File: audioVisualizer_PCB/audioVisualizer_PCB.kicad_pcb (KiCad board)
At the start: 2 copper layers, 69 x 30.5 mm, 41 parts, among them J1 Microphone_Module, J10 Conn_01x08_Socket, J11 Conn_01x08_Socket, J12 Conn_01x08_Socket, J2 USB_B_Micro, J3 SPI_MATRIX, J4 JTAG, J5 Conn_01x08_Socket, J6 Conn_01x08_Socket, J7 Conn_01x08_Socket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

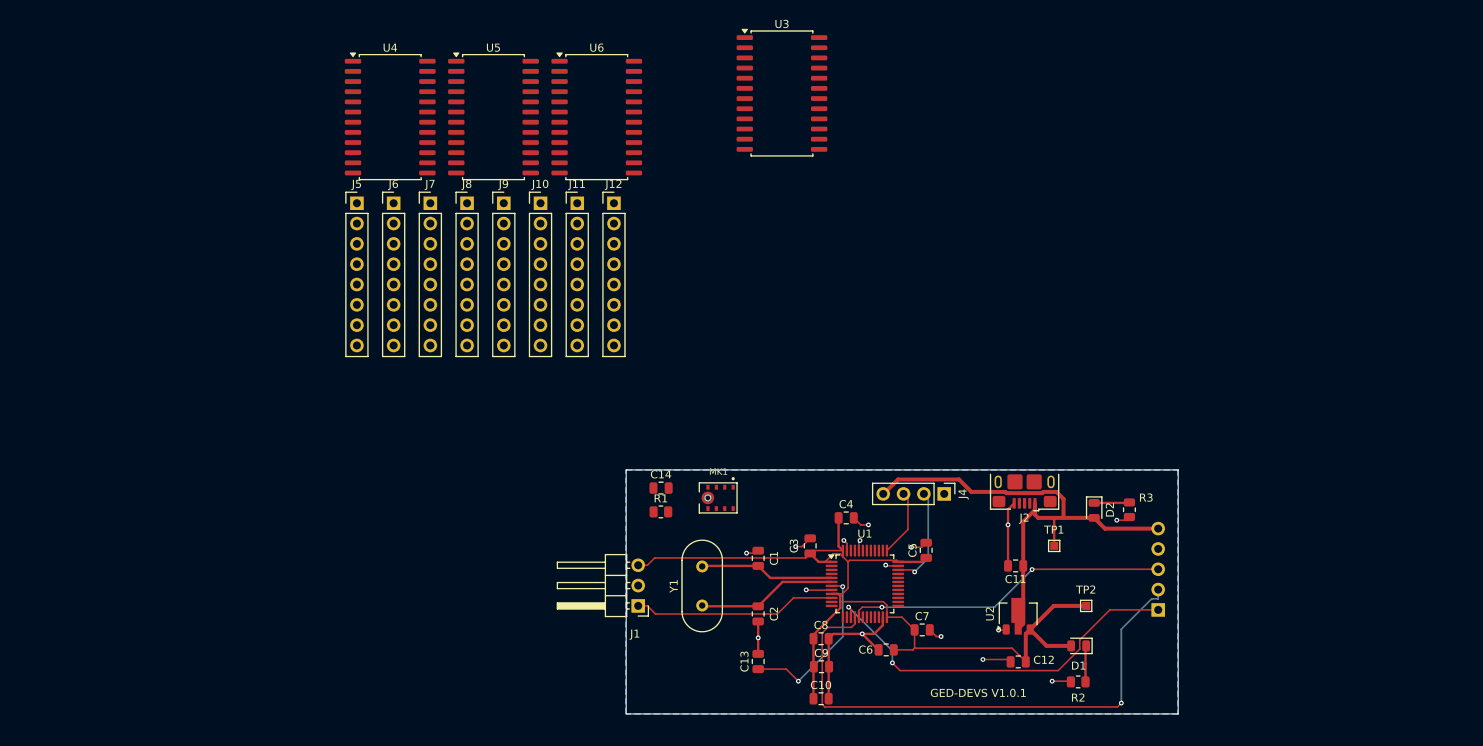
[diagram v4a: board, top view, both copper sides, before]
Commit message: migration to stm32f401
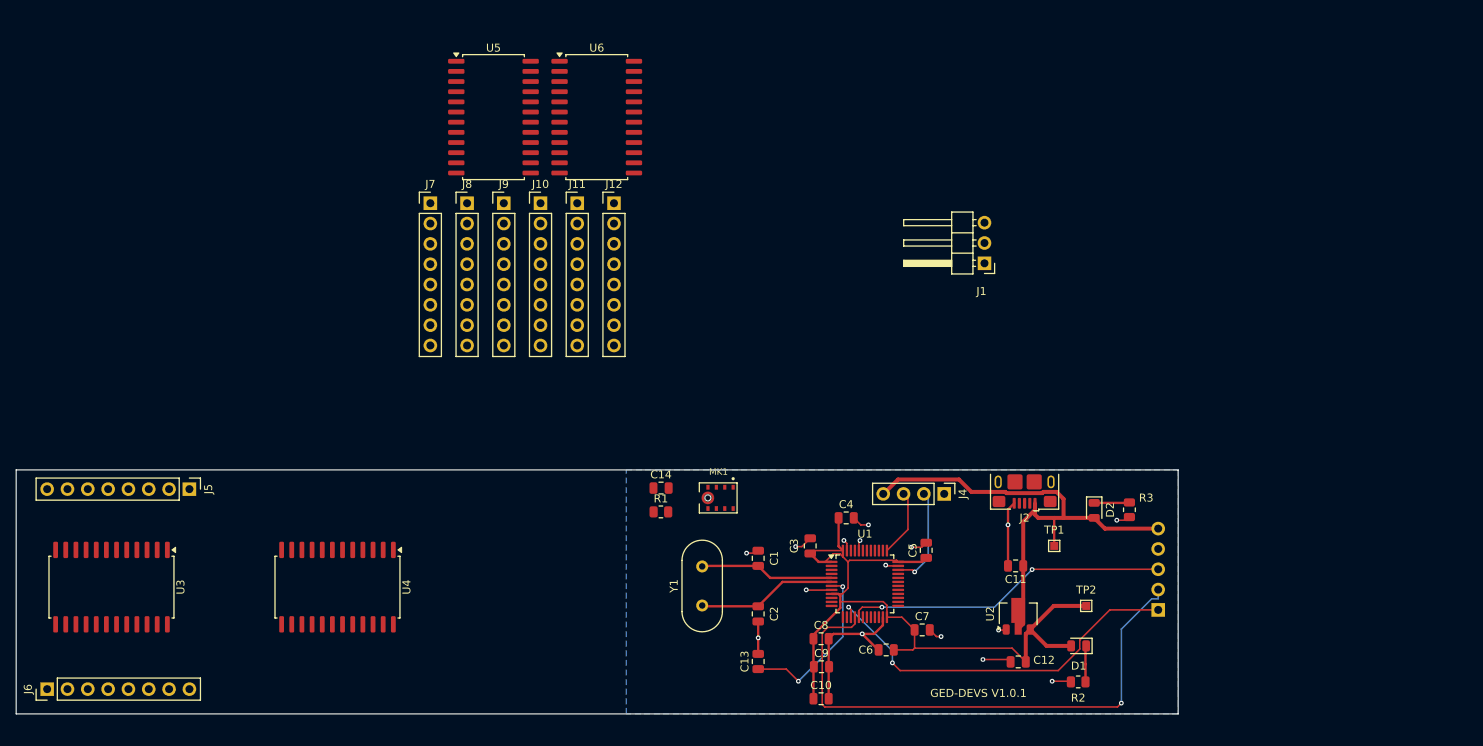
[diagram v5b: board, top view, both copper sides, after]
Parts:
- moved U3 104.1 mm to (26.2, 83.2), turned to -90 degrees
- moved J6 74.6 mm to (18.2, 96.0), turned to 90 degrees
- moved J1 60.9 mm to (135.4, 42.8)
- moved U4 59.1 mm to (54.5, 83.2), turned to -90 degrees
- moved J5 41.4 mm to (36.0, 71.0), turned to -90 degrees
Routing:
- net /OUT: track 25.4 -> 0.00 mm
- net +3.3V: track 117.8 -> 95.7 mm
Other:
- board size 69 x 30.5 mm -> 145.2 x 30.5 mm

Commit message: embeddeding the mcu is harder than I thought
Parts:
- added U7: STM32F401CCUx, Package_DFN_QFN:QFN-48-1EP_7x7mm_P0.5mm_EP5.6x5.6mm, F.Cu at (173.5, 57.2)
- added Y2: Crystal_GND23, Crystal:Crystal_SMD_3225-4Pin_3.2x2.5mm, F.Cu at (170.6, 67.7)
- moved U6 73.2 mm to (129.2, 84.3), turned to -90 degrees
- moved J12 69.5 mm to (119.7, 97.7), turned to 90 degrees
- moved C12 65.8 mm to (175.7, 37.6)
- moved C13 65.8 mm to (143.2, 37.6)
- moved C2 65.8 mm to (143.2, 31.6)
- moved C3 65.8 mm to (149.7, 23.1)
- moved C4 65.8 mm to (154.2, 19.6)
- moved C5 65.8 mm to (164.2, 23.7)
- moved C6 65.8 mm to (159.2, 36.1)
- moved C7 65.8 mm to (163.7, 33.6)
- moved C9 65.8 mm to (151.1, 38.2)
- moved D2 65.8 mm to (185.2, 18.7)
- moved J2 65.8 mm to (176.5, 15.1)
- moved J3 65.8 mm to (193.2, 31.1)
- moved J4 65.8 mm to (166.5, 16.6)
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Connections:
- C1 pad 2: Net-(U1-PD0) -> unconnected-(C1-Pad2)
- C13 pad 1: Net-(U1-NRST) -> unconnected-(C13-Pad1)
- C2 pad 1: Net-(U1-PD1) -> unconnected-(C2-Pad1)
- J10 pad 1: Net-(J10-Pin_1) -> Net-(J6-Pin_1)
- J10 pad 2: Net-(J10-Pin_2) -> Net-(J6-Pin_2)
- J10 pad 3: Net-(J10-Pin_3) -> Net-(J6-Pin_3)
- J10 pad 4: Net-(J10-Pin_4) -> Net-(J6-Pin_4)
- J10 pad 5: Net-(J10-Pin_5) -> Net-(J6-Pin_5)
- J10 pad 6: Net-(J10-Pin_6) -> Net-(J6-Pin_6)
- J10 pad 7: Net-(J10-Pin_7) -> Net-(J6-Pin_7)
- J10 pad 8: Net-(J10-Pin_8) -> Net-(J6-Pin_8)
- J11 pad 1: Net-(J11-Pin_1) -> Net-(J5-Pin_1)
- J11 pad 2: Net-(J11-Pin_2) -> Net-(J5-Pin_2)
- J11 pad 3: Net-(J11-Pin_3) -> Net-(J5-Pin_3)
- J11 pad 4: Net-(J11-Pin_4) -> Net-(J5-Pin_4)
- J11 pad 5: Net-(J11-Pin_5) -> Net-(J5-Pin_5)
- J11 pad 6: Net-(J11-Pin_6) -> Net-(J5-Pin_6)
- J11 pad 7: Net-(J11-Pin_7) -> Net-(J5-Pin_7)
- J11 pad 8: Net-(J11-Pin_8) -> Net-(J5-Pin_8)
- J12 pad 1: Net-(J12-Pin_1) -> Net-(J6-Pin_1)
- J12 pad 2: Net-(J12-Pin_2) -> Net-(J6-Pin_2)
- J12 pad 3: Net-(J12-Pin_3) -> Net-(J6-Pin_3)
- J12 pad 4: Net-(J12-Pin_4) -> Net-(J6-Pin_4)
- J12 pad 5: Net-(J12-Pin_5) -> Net-(J6-Pin_5)
- J12 pad 6: Net-(J12-Pin_6) -> Net-(J6-Pin_6)
- J12 pad 7: Net-(J12-Pin_7) -> Net-(J6-Pin_7)
- J12 pad 8: Net-(J12-Pin_8) -> Net-(J6-Pin_8)
- J7 pad 1: Net-(J7-Pin_1) -> Net-(J5-Pin_1)
- J7 pad 2: Net-(J7-Pin_2) -> Net-(J5-Pin_2)
- J7 pad 3: Net-(J7-Pin_3) -> Net-(J5-Pin_3)
- J7 pad 4: Net-(J7-Pin_4) -> Net-(J5-Pin_4)
- J7 pad 5: Net-(J7-Pin_5) -> Net-(J5-Pin_5)
- J7 pad 6: Net-(J7-Pin_6) -> Net-(J5-Pin_6)
- J7 pad 7: Net-(J7-Pin_7) -> Net-(J5-Pin_7)
- J7 pad 8: Net-(J7-Pin_8) -> Net-(J5-Pin_8)
- J8 pad 1: Net-(J8-Pin_1) -> Net-(J6-Pin_1)
- J8 pad 2: Net-(J8-Pin_2) -> Net-(J6-Pin_2)
- J8 pad 3: Net-(J8-Pin_3) -> Net-(J6-Pin_3)
- J8 pad 4: Net-(J8-Pin_4) -> Net-(J6-Pin_4)
- J8 pad 5: Net-(J8-Pin_5) -> Net-(J6-Pin_5)
- J8 pad 6: Net-(J8-Pin_6) -> Net-(J6-Pin_6)
- J8 pad 7: Net-(J8-Pin_7) -> Net-(J6-Pin_7)
- J8 pad 8: Net-(J8-Pin_8) -> Net-(J6-Pin_8)
- J9 pad 1: Net-(J9-Pin_1) -> Net-(J5-Pin_1)
- J9 pad 2: Net-(J9-Pin_2) -> Net-(J5-Pin_2)
- J9 pad 3: Net-(J9-Pin_3) -> Net-(J5-Pin_3)
- J9 pad 4: Net-(J9-Pin_4) -> Net-(J5-Pin_4)
- J9 pad 5: Net-(J9-Pin_5) -> Net-(J5-Pin_5)
- J9 pad 6: Net-(J9-Pin_6) -> Net-(J5-Pin_6)
- J9 pad 7: Net-(J9-Pin_7) -> Net-(J5-Pin_7)
- J9 pad 8: Net-(J9-Pin_8) -> Net-(J5-Pin_8)
- U4 pad 10: Net-(J8-Pin_6) -> Net-(J6-Pin_6)
- U4 pad 11: Net-(J8-Pin_2) -> Net-(J6-Pin_2)
- U4 pad 14: Net-(J7-Pin_1) -> Net-(J5-Pin_1)
- U4 pad 15: Net-(J7-Pin_6) -> Net-(J5-Pin_6)
- U4 pad 16: Net-(J7-Pin_2) -> Net-(J5-Pin_2)
- U4 pad 17: Net-(J7-Pin_7) -> Net-(J5-Pin_7)
- U4 pad 18: Net-(U4-ISET) -> Net-(U3-ISET)
- U4 pad 2: Net-(J8-Pin_1) -> Net-(J6-Pin_1)
- U4 pad 20: Net-(J7-Pin_3) -> Net-(J5-Pin_3)
- U4 pad 21: Net-(J7-Pin_5) -> Net-(J5-Pin_5)
- U4 pad 22: Net-(J7-Pin_8) -> Net-(J5-Pin_8)
- U4 pad 23: Net-(J7-Pin_4) -> Net-(J5-Pin_4)
- U4 pad 3: Net-(J8-Pin_5) -> Net-(J6-Pin_5)
- U4 pad 5: Net-(J8-Pin_7) -> Net-(J6-Pin_7)
- U4 pad 6: Net-(J8-Pin_3) -> Net-(J6-Pin_3)
- U4 pad 7: Net-(J8-Pin_4) -> Net-(J6-Pin_4)
- U4 pad 8: Net-(J8-Pin_8) -> Net-(J6-Pin_8)
- U5 pad 10: Net-(J10-Pin_6) -> Net-(J6-Pin_6)
- U5 pad 11: Net-(J10-Pin_2) -> Net-(J6-Pin_2)
- U5 pad 14: Net-(J9-Pin_1) -> Net-(J5-Pin_1)
- U5 pad 15: Net-(J9-Pin_6) -> Net-(J5-Pin_6)
- U5 pad 16: Net-(J9-Pin_2) -> Net-(J5-Pin_2)
- U5 pad 17: Net-(J9-Pin_7) -> Net-(J5-Pin_7)
- U5 pad 18: Net-(U5-ISET) -> Net-(U3-ISET)
- U5 pad 2: Net-(J10-Pin_1) -> Net-(J6-Pin_1)
- U5 pad 20: Net-(J9-Pin_3) -> Net-(J5-Pin_3)
- U5 pad 21: Net-(J9-Pin_5) -> Net-(J5-Pin_5)
- U5 pad 22: Net-(J9-Pin_8) -> Net-(J5-Pin_8)
- U5 pad 23: Net-(J9-Pin_4) -> Net-(J5-Pin_4)
- U5 pad 3: Net-(J10-Pin_5) -> Net-(J6-Pin_5)
- U5 pad 5: Net-(J10-Pin_7) -> Net-(J6-Pin_7)
- U5 pad 6: Net-(J10-Pin_3) -> Net-(J6-Pin_3)
- U5 pad 7: Net-(J10-Pin_4) -> Net-(J6-Pin_4)
- U5 pad 8: Net-(J10-Pin_8) -> Net-(J6-Pin_8)
- U6 pad 10: Net-(J12-Pin_6) -> Net-(J6-Pin_6)
- U6 pad 11: Net-(J12-Pin_2) -> Net-(J6-Pin_2)
- U6 pad 14: Net-(J11-Pin_1) -> Net-(J5-Pin_1)
- U6 pad 15: Net-(J11-Pin_6) -> Net-(J5-Pin_6)
- U6 pad 16: Net-(J11-Pin_2) -> Net-(J5-Pin_2)
- U6 pad 17: Net-(J11-Pin_7) -> Net-(J5-Pin_7)
- U6 pad 18: Net-(U6-ISET) -> Net-(U3-ISET)
- U6 pad 2: Net-(J12-Pin_1) -> Net-(J6-Pin_1)
- U6 pad 20: Net-(J11-Pin_3) -> Net-(J5-Pin_3)
- U6 pad 21: Net-(J11-Pin_5) -> Net-(J5-Pin_5)
- U6 pad 22: Net-(J11-Pin_8) -> Net-(J5-Pin_8)
- U6 pad 23: Net-(J11-Pin_4) -> Net-(J5-Pin_4)
- U6 pad 3: Net-(J12-Pin_5) -> Net-(J6-Pin_5)
- U6 pad 5: Net-(J12-Pin_7) -> Net-(J6-Pin_7)
- U6 pad 6: Net-(J12-Pin_3) -> Net-(J6-Pin_3)
- U6 pad 7: Net-(J12-Pin_4) -> Net-(J6-Pin_4)
- U6 pad 8: Net-(J12-Pin_8) -> Net-(J6-Pin_8)
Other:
- board size 145.2 x 30.5 mm -> 129.1 x 32.5 mm

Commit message: added stereo mics; setup usb-c;fixed timer issue for led matrix; using external clock
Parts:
- removed C1, C2: 20p, Capacitor_SMD:C_0805_2012Metric
- removed J10, J11, J12, J5, J6, J7, J8, J9: Conn_01x08_Socket, Connector_PinHeader_2.54mm:PinHeader_1x08_P2.54mm_Vertical
- removed U1: STM32F103C8Tx, Package_QFP:LQFP-48_7x7mm_P0.5mm
- removed U3, U4, U5, U6: MAX7219, Package_SO:SOIC-24W_7.5x15.4mm_P1.27mm
- removed Y1: 8Mhz, Crystal:Crystal_HC49-4H_Vertical
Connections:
- U7 pad 5: unconnected-(U7-PH0-Pad5) -> Net-(U7-PH0)
- Y2 pad 2: GND -> (no net)
- Y2 pad 3: GND -> Net-(U7-PH0)
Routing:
- net (no net): track 0.00 -> 34.3 mm
- net unconnected-(C13-Pad1): track 0.00 -> 21.2 mm, vias 0 -> 2
- net Net-(U1-NRST): track 21.2 -> 0.00 mm, vias 2 -> 0
- net Net-(U1-PD1): track 17.5 -> 0.00 mm
- net Net-(U1-PD0): track 16.8 -> 0.00 mm

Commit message: finished pcb ready for production
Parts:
- removed D2: LED, LED_SMD:LED_0805_2012Metric
- removed J2: USB_B_Micro, Connector_USB:USB_Micro-B_Amphenol_10118193-0001LF_Horizontal
- removed J4: JTAG, Connector_PinHeader_2.54mm:PinHeader_1x04_P2.54mm_Vertical
- removed MK1: INMP441ACEZ-R7, Microphone:MIC_INMP441ACEZ-R7
- removed Y2: Crystal_GND23, Crystal:Crystal_SMD_3225-4Pin_3.2x2.5mm
- added C1: 15pF, Capacitor_SMD:C_0805_2012Metric, F.Cu at (76.0, 84.0)
- added C15: 1uF, Capacitor_SMD:C_0805_2012Metric, B.Cu at (35.0, 98.5)
- added C16: 100nF, Capacitor_SMD:C_0805_2012Metric, F.Cu at (133.0, 80.0)
- added C17: 1uF, Capacitor_SMD:C_0805_2012Metric, F.Cu at (127.5, 80.0)
- added MK-L1: INMP441-L, Custom:MIC_INMP441ACEZ-R7, F.Cu at (25.5, 76.0)
- added MK-R1: INMP441-R, Custom:MIC_INMP441ACEZ-R7, F.Cu at (140.3, 76.2)
- added R29: 100k, Resistor_SMD:R_0805_2012Metric, F.Cu at (95.9, 87.0)
- added TP3: SWDIO, TestPoint:TestPoint_Pad_1.0x1.0mm, B.Cu at (103.5, 71.5)
- added TP4: SWCLK, TestPoint:TestPoint_Pad_1.0x1.0mm, B.Cu at (97.5, 71.5)
- added TP5: TestPoint_5V, TestPoint:TestPoint_Pad_1.0x1.0mm, B.Cu at (111.0, 71.5)
- added Y1: ASE-25MHz, Oscillator:Oscillator_SMD_Abracon_ASE-4Pin_3.2x2.5mm, F.Cu at (70.0, 86.7)
- added kibuzzard-69F6314F: G***, kibuzzard-69F6314F, B.Cu at (127.5, 71.5)
- C10, C9: value 1u -> 1uF
- C14: value C -> 100nF; moved to B.Cu
- C3, C4, C5, C6: value 100n -> 100nF
- C7: value 10u -> 10uF
- C8: value 10n -> 10nF
- J1: value Microphone_Module -> USB_C_Receptacle_USB2.0_16P; footprint Connector_PinHeader_2.54mm:PinHeader_1x03_P2.54mm_Horizontal -> Connector_USB:USB_C_Receptacle_GCT_USB4105-xx-A_16P_TopMnt_Horizontal; moved to B.Cu
- J3: value SPI_MATRIX -> SPI_LED_MATRIX; moved to F.Cu
- R1: value R -> 5.1; moved to B.Cu
- R3: value 100 -> 5.1; moved to B.Cu
- TP1, TP2: moved to B.Cu
- moved R3 177.2 mm to (30.0, 95.5), turned to 180 degrees
- moved TP1 156.8 mm to (43.0, 99.0)
- moved C11 145.9 mm to (44.5, 90.0)
- moved U2 140.8 mm to (45.0, 84.0)
- moved TP2 138.5 mm to (53.0, 75.0)
- moved D1 137.4 mm to (53.9, 82.0)
- moved R2 135.3 mm to (56.5, 87.5), turned to -90 degrees
- moved C12 134.3 mm to (51.0, 87.5), turned to -90 degrees
- moved C14 130.5 mm to (30.0, 98.5), turned to 180 degrees
- moved R1 124.8 mm to (29.9, 92.0), turned to 180 degrees
- moved J1 116.0 mm to (20.6, 95.2), turned to 90 degrees
- moved C5 103.6 mm to (77.0, 79.5)
- moved C4 98.8 mm to (86.5, 91.5), turned to 180 degrees
- moved U7 94.3 mm to (83.4, 84.8)
- moved C9 89.7 mm to (76.5, 88.0), turned to -90 degrees
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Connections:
- C11 pad 1: VBUS -> +5V
- C13 pad 1: unconnected-(C13-Pad1) -> Net-(U7-NRST)
- C14 pad 1: unconnected-(C14-Pad1) -> GND
- C14 pad 2: unconnected-(C14-Pad2) -> +5V
- J3 pad 1: /CLK -> +5V
- J3 pad 2: /CS -> GND
- J3 pad 3: /DIN -> Net-(J3-DIN)
- J3 pad 4: GND -> Net-(J3-CS)
- J3 pad 5: VBUS -> Net-(J3-CLK)
- R1 pad 1: unconnected-(R1-Pad1) -> GND
- R1 pad 2: unconnected-(R1-Pad2) -> Net-(J1-CC2)
- R3 pad 2: Net-(D2-K) -> Net-(J1-CC1)
- TP1 pad 1: VBUS -> +5V
- U2 pad 2: VBUS -> +5V
- U7 pad 15: unconnected-(U7-PA5-Pad15) -> Net-(J3-CLK)
- U7 pad 16: unconnected-(U7-PA6-Pad16) -> Net-(J3-CS)
- U7 pad 17: unconnected-(U7-PA7-Pad17) -> Net-(J3-DIN)
- U7 pad 21: unconnected-(U7-PB10-Pad21) -> MIC_SCK
- U7 pad 25: unconnected-(U7-PB12-Pad25) -> MIC_WS
- U7 pad 28: unconnected-(U7-PB15-Pad28) -> MIC_SD
- U7 pad 32: unconnected-(U7-PA11-Pad32) -> USB_DM
- U7 pad 33: unconnected-(U7-PA12-Pad33) -> USB_DP
- U7 pad 34: unconnected-(U7-PA13-Pad34) -> Net-(U7-PA13)
- U7 pad 37: unconnected-(U7-PA14-Pad37) -> Net-(U7-PA14)
- U7 pad 44: unconnected-(U7-BOOT0-Pad44) -> GND
- U7 pad 7: unconnected-(U7-NRST-Pad7) -> Net-(U7-NRST)
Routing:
- net GND: track 58.2 -> 310.7 mm, vias 16 -> 3
- net +5V: track 0.00 -> 173.9 mm, vias 0 -> 3
- net MIC_SCK: track 0.00 -> 134.0 mm, vias 0 -> 3
- net MIC_SD: track 0.00 -> 131.1 mm, vias 0 -> 3
- net MIC_WS: track 0.00 -> 126.8 mm, vias 0 -> 3
- net +3.3V: track 95.7 -> 210.9 mm, vias 0 -> 5
- net USB_DP: track 0.00 -> 79.0 mm, vias 0 -> 1
- net USB_DM: track 0.00 -> 77.4 mm, vias 0 -> 1
- net /CS: track 68.6 -> 0.00 mm, vias 1 -> 0
- net Net-(J3-DIN): track 0.00 -> 65.8 mm
- net Net-(J3-CLK): track 0.00 -> 65.1 mm
- net VBUS: track 62.8 -> 0.00 mm
- net /CLK: track 48.0 -> 0.00 mm, vias 2 -> 0
- net /DIN: track 40.4 -> 0.00 mm, vias 2 -> 0
- net (no net): track 34.3 -> 0.00 mm
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- removed copper zone on B.Cu, net GND
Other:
- board text removed: "GED-DEVS V1.0.1"
- board text removed: "VBUS GND DIN CS CLK"
